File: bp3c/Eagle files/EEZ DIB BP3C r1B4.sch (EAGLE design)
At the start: 26 parts, among them Q1 IRLML6244TRPBF, Q2 IRLML6244TRPBF, X1 ZL202-20G, X2 ZL202-20G, X3 ZL202-20G, X4 ZL212-40KG, X5 TSW-113-07-F-D, X6 TSW-113-07-F-D, X7 TSW-113-07-F-D

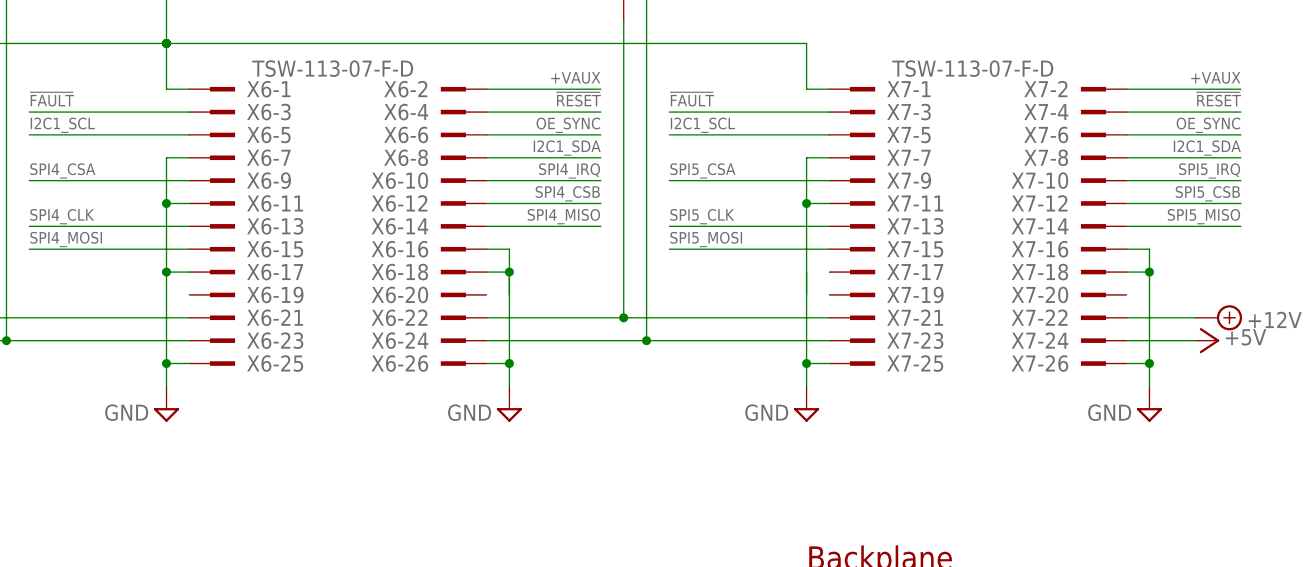
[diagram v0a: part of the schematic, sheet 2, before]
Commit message: BP3C module addressing fix
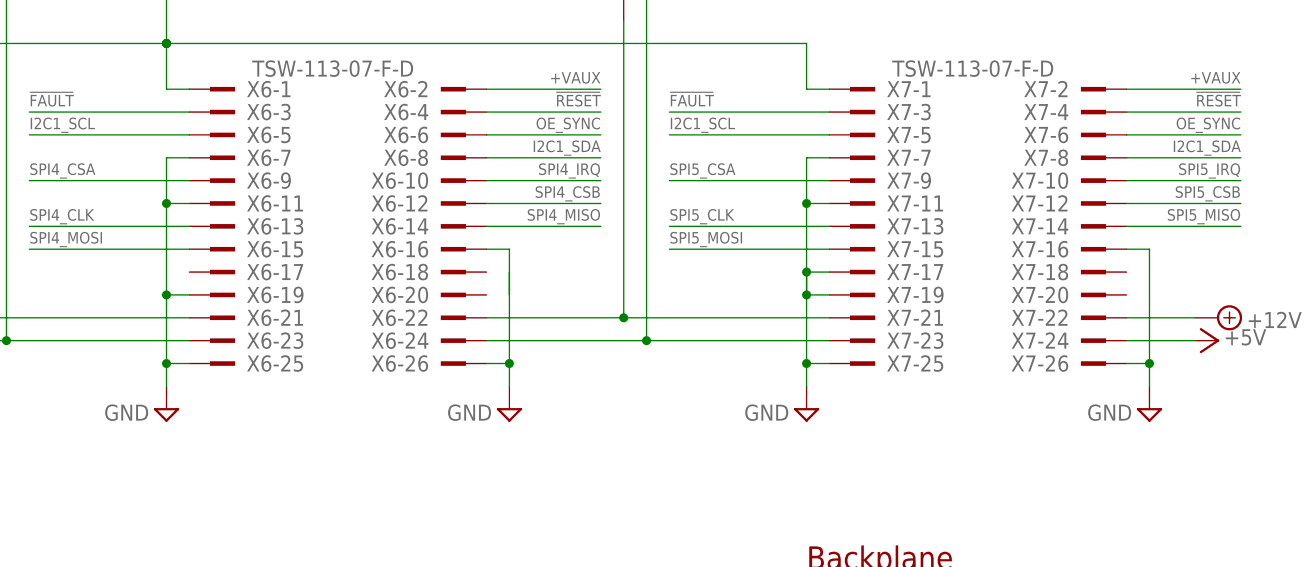
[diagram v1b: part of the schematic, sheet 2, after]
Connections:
- net GND: now also X6-19.1, X7-17.1, X7-19.1; no longer X6-17.1, X6-18.1, X7-18.1
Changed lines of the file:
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@@
 <segment>
 <wire x1="200.66" y1="50.8" x2="203.2" y2="50.8" width="0.1524" layer="91"/>
-<wire x1="203.2" y1="50.8" x2="203.2" y2="60.96" width="0.1524" layer="91"/>
-<wire x1="203.2" y1="60.96" x2="203.2" y2="63.5" width="0.1524" layer="91"/>
+<wire x1="203.2" y1="50.8" x2="203.2" y2="63.5" width="0.1524" layer="91"/>
 <wire x1="203.2" y1="63.5" x2="200.66" y2="63.5" width="0.1524" layer="91"/>
-<wire x1="200.66" y1="60.96" x2="203.2" y2="60.96" width="0.1524" layer="91"/>
-<junction x="203.2" y="60.96"/>
 <pinref part="X7" gate="-16" pin="1"/>
-<pinref part="X7" gate="-18" pin="1"/>
 <pinref part="X7" gate="-26" pin="1"/>
 <pinref part="SUPPLY19" gate="GND" pin="GND"/>
@@
 <segment>
 <wire x1="167.64" y1="50.8" x2="165.1" y2="50.8" width="0.1524" layer="91"/>
-<wire x1="165.1" y1="50.8" x2="165.1" y2="68.58" width="0.1524" layer="91"/>
+<wire x1="165.1" y1="50.8" x2="165.1" y2="58.42" width="0.1524" layer="91"/>
+<wire x1="165.1" y1="58.42" x2="165.1" y2="60.96" width="0.1524" layer="91"/>
+<wire x1="165.1" y1="60.96" x2="165.1" y2="68.58" width="0.1524" layer="91"/>
 <wire x1="165.1" y1="68.58" x2="165.1" y2="73.66" width="0.1524" layer="91"/>
 <wire x1="167.64" y1="73.66" x2="165.1" y2="73.66" width="0.1524" layer="91"/>
@@
 <wire x1="165.1" y1="48.26" x2="165.1" y2="50.8" width="0.1524" layer="91"/>
 <junction x="165.1" y="50.8"/>
+<pinref part="X7" gate="-17" pin="1"/>
+<wire x1="167.64" y1="60.96" x2="165.1" y2="60.96" width="0.1524" layer="91"/>
+<junction x="165.1" y="60.96"/>
+<pinref part="X7" gate="-19" pin="1"/>
+<wire x1="167.64" y1="58.42" x2="165.1" y2="58.42" width="0.1524" layer="91"/>
+<junction x="165.1" y="58.42"/>
 </segment>
 <segment>
 <wire x1="129.54" y1="50.8" x2="132.08" y2="50.8" width="0.1524" layer="91"/>
-<wire x1="132.08" y1="50.8" x2="132.08" y2="60.96" width="0.1524" layer="91"/>
-<wire x1="132.08" y1="60.96" x2="132.08" y2="63.5" width="0.1524" layer="91"/>
-<wire x1="129.54" y1="60.96" x2="132.08" y2="60.96" width="0.1524" layer="91"/>
-<junction x="132.08" y="60.96"/>
+<wire x1="132.08" y1="50.8" x2="132.08" y2="63.5" width="0.1524" layer="91"/>
 <wire x1="129.54" y1="63.5" x2="132.08" y2="63.5" width="0.1524" layer="91"/>
 <pinref part="X6" gate="-16" pin="1"/>
-<pinref part="X6" gate="-18" pin="1"/>
 <pinref part="X6" gate="-26" pin="1"/>
 <pinref part="SUPPLY15" gate="GND" pin="GND"/>
@@
 <segment>
 <wire x1="96.52" y1="50.8" x2="93.98" y2="50.8" width="0.1524" layer="91"/>
-<wire x1="93.98" y1="50.8" x2="93.98" y2="60.96" width="0.1524" layer="91"/>
-<wire x1="93.98" y1="60.96" x2="93.98" y2="68.58" width="0.1524" layer="91"/>
+<wire x1="93.98" y1="50.8" x2="93.98" y2="58.42" width="0.1524" layer="91"/>
+<wire x1="93.98" y1="58.42" x2="93.98" y2="68.58" width="0.1524" layer="91"/>
 <wire x1="93.98" y1="68.58" x2="93.98" y2="73.66" width="0.1524" layer="91"/>
 <wire x1="96.52" y1="73.66" x2="93.98" y2="73.66" width="0.1524" layer="91"/>
@@
 <junction x="93.98" y="50.8"/>
 <pinref part="SUPPLY13" gate="GND" pin="GND"/>
-<pinref part="X6" gate="-17" pin="1"/>
-<wire x1="96.52" y1="60.96" x2="93.98" y2="60.96" width="0.1524" layer="91"/>
-<junction x="93.98" y="60.96"/>
+<pinref part="X6" gate="-19" pin="1"/>
+<wire x1="96.52" y1="58.42" x2="93.98" y2="58.42" width="0.1524" layer="91"/>
+<junction x="93.98" y="58.42"/>
 </segment>
 <segment>
